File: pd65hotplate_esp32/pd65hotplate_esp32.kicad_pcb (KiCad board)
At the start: 2 copper layers, 22 parts, among them IC1 LMR36510FADDAR, U2 ESP32-S3-WROOM-1U-N16R8, U3 STUSB4500QTR, U4 HUSB238_002DD, U6 HUSB238A

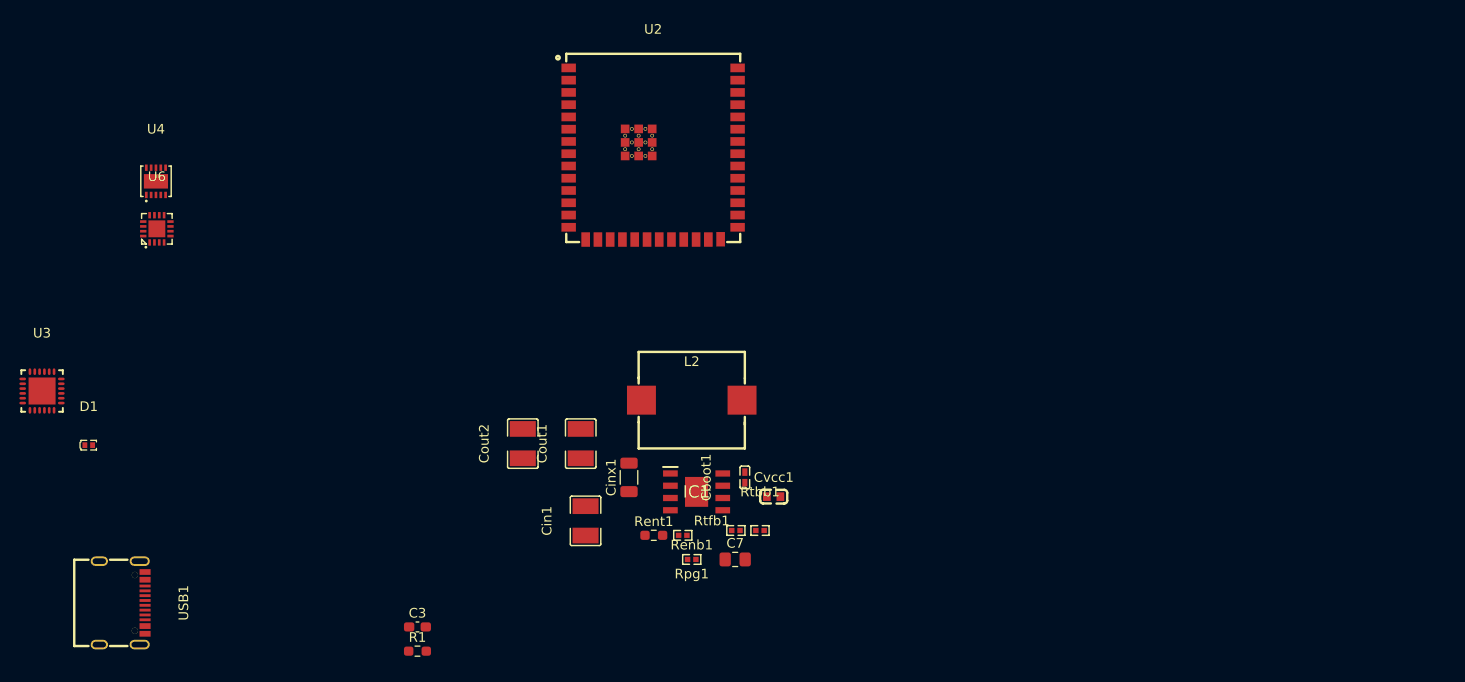
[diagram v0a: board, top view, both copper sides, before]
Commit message: add supercap backup
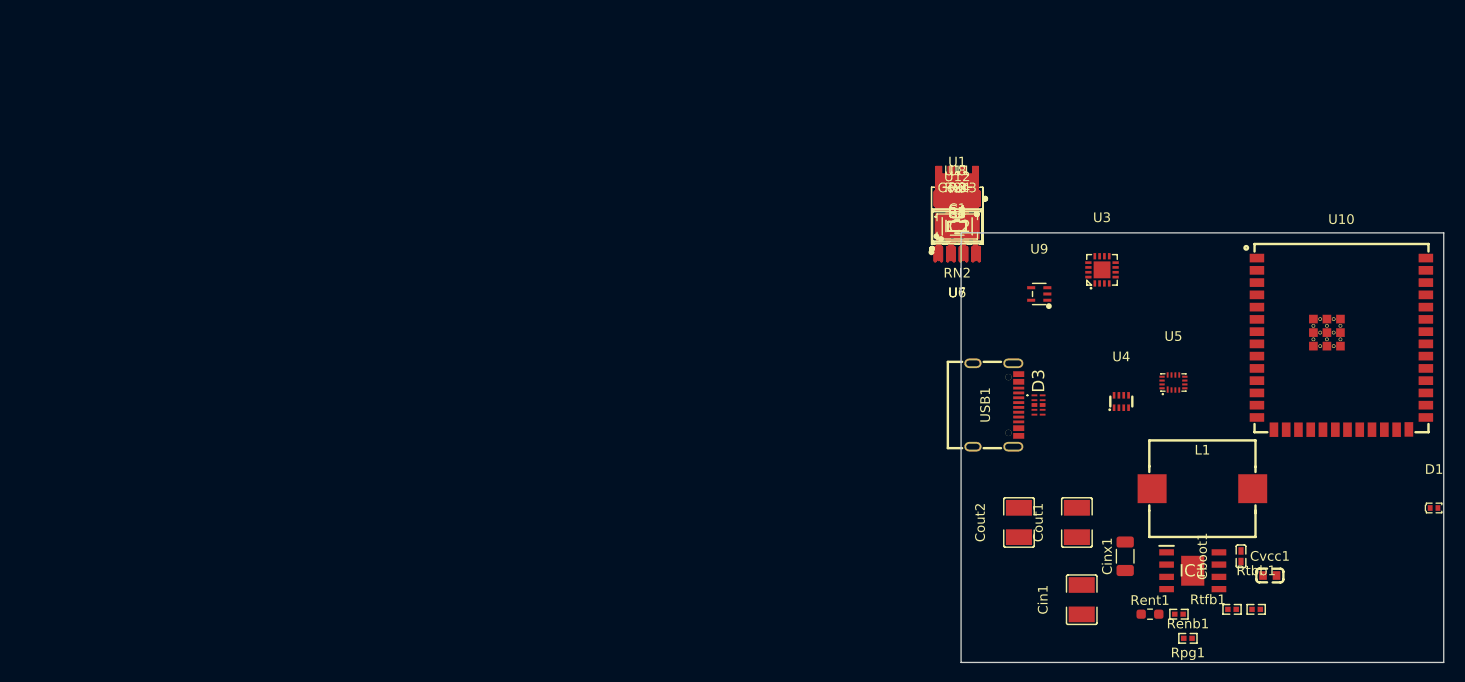
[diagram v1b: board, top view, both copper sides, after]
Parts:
- removed C7: 22p, Capacitor_SMD:C_0805_2012Metric_Pad1.18x1.45mm_HandSolder
- removed L2: SDR1105-220ML, easyeda2kicad:IND-SMD_L11.0-W10.0-2
- removed U2: ESP32-S3-WROOM-1U-N16R8, easyeda2kicad:WIRELM-SMD_ESP32-S3-WROOM-1U
- added C1: 220n/100V, Capacitor_SMD:C_1206_3216Metric, F.Cu at (138.0, 44.0)
- added C4: 22p, Capacitor_SMD:C_0805_2012Metric_Pad1.18x1.45mm_HandSolder, F.Cu at (138.0, 44.0)
- added Cout3: GRM32ER61C476KE15L, easyeda2kicad:C1210, F.Cu at (138.0, 44.0)
- added D3: PESD4USB5U-TTSX, SamacSys_Parts:PESD4USB5UTTSX, F.Cu at (146.4, 62.5)
- added IC2: BQ25173QWDRCRQ1, SamacSys_Parts:BQ25173QWDRCRQ1, F.Cu at (138.0, 44.0)
- added L1: SDR1105-220ML, easyeda2kicad:IND-SMD_L11.0-W10.0-2, F.Cu at (163.4, 71.2)
- added R2: 50k, easyeda2kicad:R0402, F.Cu at (138.0, 44.0)
- added R24: 10k, easyeda2kicad:R0402, F.Cu at (138.0, 44.0)
- added R3: 10R, Resistor_SMD:R_0603_1608Metric_Pad0.98x0.95mm_HandSolder, F.Cu at (138.0, 44.0)
- added R4, R7, R8: 900k, Resistor_SMD:R_0603_1608Metric_Pad0.98x0.95mm_HandSolder, F.Cu at (138.0, 44.0)
- added R5: ~, Resistor_SMD:R_0603_1608Metric_Pad0.98x0.95mm_HandSolder, F.Cu at (138.0, 44.0)
- added R6: ~, easyeda2kicad:R0402, F.Cu at (138.0, 44.0)
- added RN2: 100k, easyeda2kicad:RES-ARRAY-SMD_16P-L3.8-W1.6-P0.50-BL, F.Cu at (138.0, 44.0)
- added U1: RT9068GSP, easyeda2kicad:ESOP-8_L4.9-W3.9-P1.27-LS6.0-BL-EP2.3, F.Cu at (138.0, 44.0)
- added U10: ESP32-S3-WROOM-1U-N16R8, easyeda2kicad:WIRELM-SMD_ESP32-S3-WROOM-1U, F.Cu at (177.8, 56.2)
- added U11, U8: AGM60P90A, easyeda2kicad:TDSON-8_L5.9-W5.2-P1.27-BL, F.Cu at (138.0, 44.0)
- added U12: SY6280AAAC, easyeda2kicad:TSOT-23-5_L2.9-W1.6-P0.95-LS2.8-BL, F.Cu at (138.0, 44.0)
- added U5: FSA2567UMX, easyeda2kicad:UMLP-16_L2.6-W1.8-P0.40-BL, F.Cu at (160.4, 60.2)
- added U7: 74HC4051PW,118, easyeda2kicad:TSSOP-16_L5.0-W4.4-P0.65-LS6.4-BL, F.Cu at (138.0, 44.0)
- added U9: 74AHC1G14SE-7, easyeda2kicad:SOT-353_L2.1-W1.3-P0.65-LS2.3-BR, F.Cu at (146.5, 51.0)
- R1: value 10R -> 920k
- U3: value STUSB4500QTR -> HUSB238A; footprint easyeda2kicad:QFN-24_L4.0-W4.0-P0.50-BL-EP2.8 -> easyeda2kicad:QFN-16_L3.0-W3.0-P0.50-BL-EP1.7
- U4: value HUSB238_002DD -> LM66200DRLR; footprint easyeda2kicad:DFN-10_L3.0-W3.0-P0.50-BL-EP2.5 -> easyeda2kicad:SOT-583-8_L2.1-W1.2-P0.50-LS1.6-BL
- U6: value HUSB238A -> 74HC4051PW,118; footprint easyeda2kicad:QFN-16_L3.0-W3.0-P0.50-BL-EP1.7 -> easyeda2kicad:TSSOP-16_L5.0-W4.4-P0.65-LS6.4-BL
- moved D1 139.5 mm to (187.4, 73.2)
- moved U3 110.5 mm to (153.0, 48.5)
- moved U4 102.6 mm to (155.0, 62.1)
- moved USB1 92.8 mm to (142.0, 62.5)
- moved U6 82.9 mm to (138.0, 44.0), turned to 180 degrees
- moved R1 71.1 mm to (138.0, 44.0)
- moved C3 69.6 mm to (138.0, 44.0)
- moved Cboot1 52.0 mm to (167.4, 78.2)
- moved Cin1 52.0 mm to (150.9, 82.7)
- moved Cinx1 52.0 mm to (155.4, 78.2)
- moved Cout1 52.0 mm to (150.4, 74.7)
- moved Cout2 52.0 mm to (144.4, 74.7)
- moved IC1 52.0 mm to (162.4, 79.7)
- moved Renb1 52.0 mm to (161.0, 84.2)
- moved Rent1 52.0 mm to (158.0, 84.2)
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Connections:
- Cout1 pad 2: 3V3 -> Net-(U1-SENSE)
- Cout2 pad 2: 3V3 -> 3V3smps
- R1 pad 1: Vbus -> Net-(U1-SENSE)
- R1 pad 2: Net-(U4-VIN) -> Net-(U1-FB)
- Rpg1 pad 2: 3V3 -> 3V3smps
- Rtfb1 pad 1: 3V3 -> 3V3smps
- U3 pad 1: unconnected-(U3-CC1DB-Pad1) -> DP
- U3 pad 10: unconnected-(U3-GND-Pad10) -> Net-(U3-SCL/SNK_ISET)
- U3 pad 11: unconnected-(U3-ATTACH-Pad11) -> INT
- U3 pad 12: unconnected-(U3-ADDR0-Pad12) -> ENnPD
- U3 pad 15: unconnected-(U3-GPIO-Pad15) -> Net-(U3-GATE)
- U3 pad 16: unconnected-(U3-VBUS_EN_SNK-Pad16) -> Net-(U3-VBUS)
- U3 pad 17: unconnected-(U3-A_B_SIDE-Pad17) -> GND
- U3 pad 2: unconnected-(U3-CC1-Pad2) -> DN
- U3 pad 3: unconnected-(U3-NC-Pad3) -> CC1
- U3 pad 4: unconnected-(U3-CC2-Pad4) -> CC2
- U3 pad 5: unconnected-(U3-CC2DB-Pad5) -> 3V3
- U3 pad 6: unconnected-(U3-RESET-Pad6) -> Net-(U3-DBG_N)
- U3 pad 7: unconnected-(U3-SCL-Pad7) -> Net-(U3-EN_HVDCP/OUT1)
- U3 pad 8: unconnected-(U3-SDA-Pad8) -> Net-(U3-ADDR/ORIENT)
- U3 pad 9: unconnected-(U3-DISCH-Pad9) -> Net-(U3-SDA/SNK_VSET)
- U4 pad 1: Net-(U4-VIN) -> GND
- U4 pad 2: DP -> 3V3
- U4 pad 3: DN -> 3V3smps
- U4 pad 4: CC1 -> GND
- U4 pad 5: CC2 -> GND
- U4 pad 6: SDA -> 3V3bck
- U4 pad 7: SCL -> 3V3
- U4 pad 8: unconnected-(U4-VSET-Pad8) -> pwrsrc_ind
- U6 pad 1: DP -> Net-(U6-Y4)
- U6 pad 10: SCL -> Net-(RN2B-R2.1)
- U6 pad 11: unconnected-(U6-INT_N-Pad11) -> Net-(RN2A-R1.1)
- U6 pad 12: unconnected-(U6-EN_N-Pad12) -> Net-(U6-Y3)
- U6 pad 13: unconnected-(U6-FAULT/OUT2-Pad13) -> Net-(U6-Y0)
- U6 pad 14: unconnected-(U6-FLGIN-Pad14) -> Net-(U6-Y1)
- U6 pad 15: unconnected-(U6-GATE-Pad15) -> Net-(U6-Y2)
- U6 pad 16: Net-(U4-VIN) -> 3V3
- U6 pad 2: DN -> unconnected-(U6-Y6-Pad2)
- U6 pad 3: CC1 -> Net-(U5-2RST)
- U6 pad 4: CC2 -> GND
- U6 pad 6: unconnected-(U6-DBG_N-Pad6) -> GND
- U6 pad 7: unconnected-(U6-EN_HVDCP/OUT1-Pad7) -> GND
- U6 pad 8: unconnected-(U6-ADDR/ORIENT-Pad8) -> GND
- U6 pad 9: SDA -> Net-(RN2C-R3.1)
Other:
- board outline added: 50 x 44.5 mm
